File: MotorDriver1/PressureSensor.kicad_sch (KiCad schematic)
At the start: 6 parts

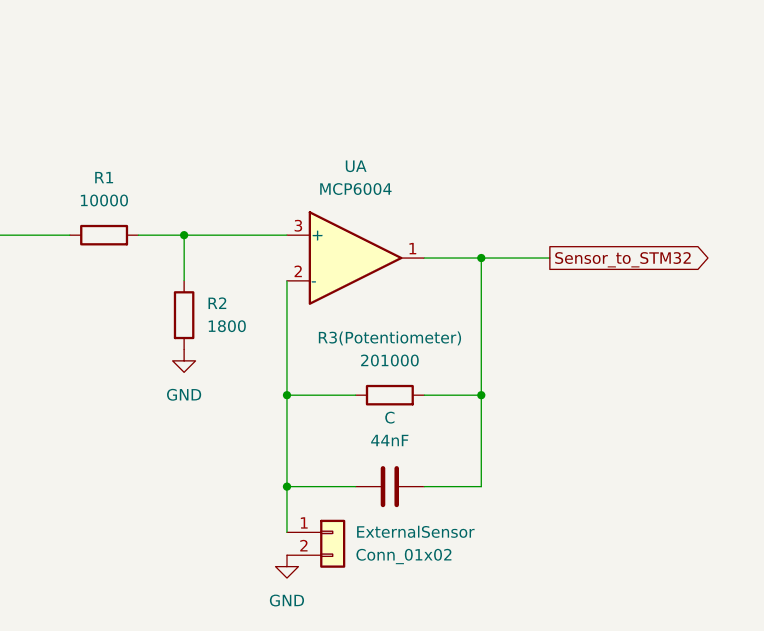
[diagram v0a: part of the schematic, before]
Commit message: added op amp rails
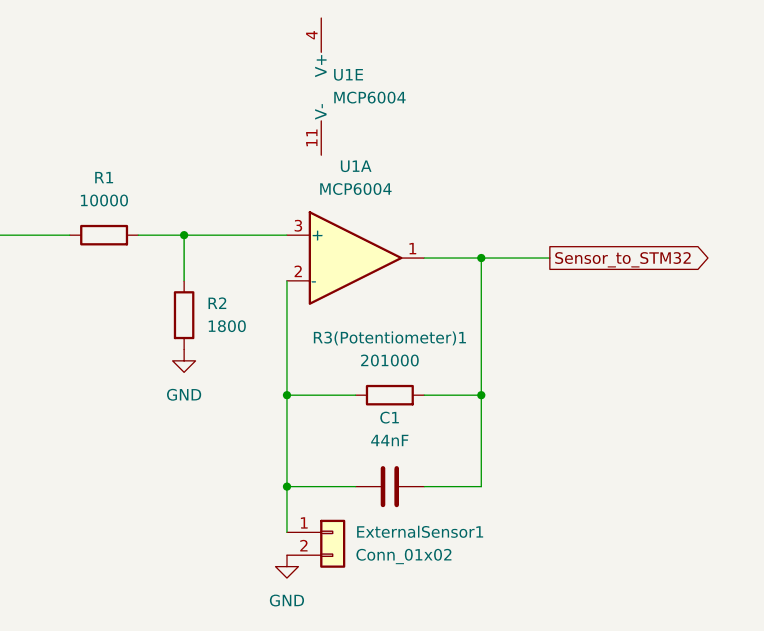
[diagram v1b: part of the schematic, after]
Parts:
- added unit 5 of U1
- renumbered C to C1, ExternalSensor to ExternalSensor1, R3(Potentiometer) to R3(Potentiometer)1, U to U1
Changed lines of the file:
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@@
 		(dnp no)
 		(fields_autoplaced yes)
-		(property "Reference" "ExternalSensor"
+		(property "Reference" "ExternalSensor1"
 			(at 130.81 118.1099 0)
 			(effects
@@
 			(project "PressureSensor"
 				(path "/6b4e6891-da04-4823-bd63-d61c29aaa975"
-					(reference "ExternalSensor")
+					(reference "ExternalSensor1")
 					(unit 1)
 				)
@@
 		(dnp no)
 		(fields_autoplaced yes)
-		(property "Reference" "U"
+		(property "Reference" "U1"
 			(at 130.81 77.47 0)
 			(effects
@@
 			(project "PressureSensor"
 				(path "/6b4e6891-da04-4823-bd63-d61c29aaa975"
-					(reference "U")
+					(reference "U1")
 					(unit 1)
 				)
@@
 	)
 	(symbol
+		(lib_id "Amplifier_Operational:MCP6004")
+		(at 129.54 68.58 0)
+		(unit 5)
+		(exclude_from_sim no)
+		(in_bom yes)
+		(on_board yes)
+		(dnp no)
+		(fields_autoplaced yes)
+		(property "Reference" "U1"
+			(at 128.27 67.3099 0)
+			(effects
+				(font
+					(size 1.27 1.27)
+				)
+				(justify left)
+			)
+		)
+		(property "Value" "MCP6004"
+			(at 128.27 69.8499 0)
+			(effects
+				(font
+					(size 1.27 1.27)
+				)
+				(justify left)
+			)
+		)
+		(property "Footprint" ""
+			(at 128.27 66.04 0)
+			(effects
+				(font
+					(size 1.27 1.27)
+				)
+				(hide yes)
+			)
+		)
+		(property "Datasheet" "http://ww1.microchip.com/downloads/en/DeviceDoc/21733j.pdf"
+			(at 130.81 63.5 0)
+			(effects
+				(font
+					(size 1.27 1.27)
+				)
+				(hide yes)
+			)
+		)
+		(property "Description" "1MHz, Low-Power Op Amp, DIP-14/SOIC-14/TSSOP-14"
+			(at 129.54 68.58 0)
+			(effects
+				(font
+					(size 1.27 1.27)
+				)
+				(hide yes)
+			)
+		)
+		(pin "13"
+		)
+		(pin "11"
+		)
+		(pin "6"
+		)
+		(pin "5"
+		)
+		(pin "1"
+		)
+		(pin "7"
+		)
+		(pin "9"
+		)
+		(pin "4"
+		)
+		(pin "8"
+		)
+		(pin "10"
+		)
+		(pin "12"
+		)
+		(pin "3"
+		)
+		(pin "2"
+		)
+		(pin "14"
+		)
+		(instances
+			(project ""
+				(path "/6b4e6891-da04-4823-bd63-d61c29aaa975"
+					(reference "U1")
+					(unit 5)
+				)
+			)
+		)
+	)
+	(symbol
 		(lib_id "Device:C")
 		(at 134.62 113.03 90)
@@
 		(dnp no)
 		(fields_autoplaced yes)
-		(property "Reference" "C"
+		(property "Reference" "C1"
 			(at 134.62 105.41 90)
 			(effects
@@
 			(project "PressureSensor"
 				(path "/6b4e6891-da04-4823-bd63-d61c29aaa975"
-					(reference "C")
+					(reference "C1")
 					(unit 1)
 				)
@@
 		(dnp no)
 		(fields_autoplaced yes)
-		(property "Reference" "R3(Potentiometer)"
+		(property "Reference" "R3(Potentiometer)1"
 			(at 134.62 96.52 90)
 			(effects
@@
 			(project "PressureSensor"
 				(path "/6b4e6891-da04-4823-bd63-d61c29aaa975"
-					(reference "R3(Potentiometer)")
-					(unit 1)
-				)
+					(reference "R3(Potentiometer)1")
+					(unit 1)
+				)

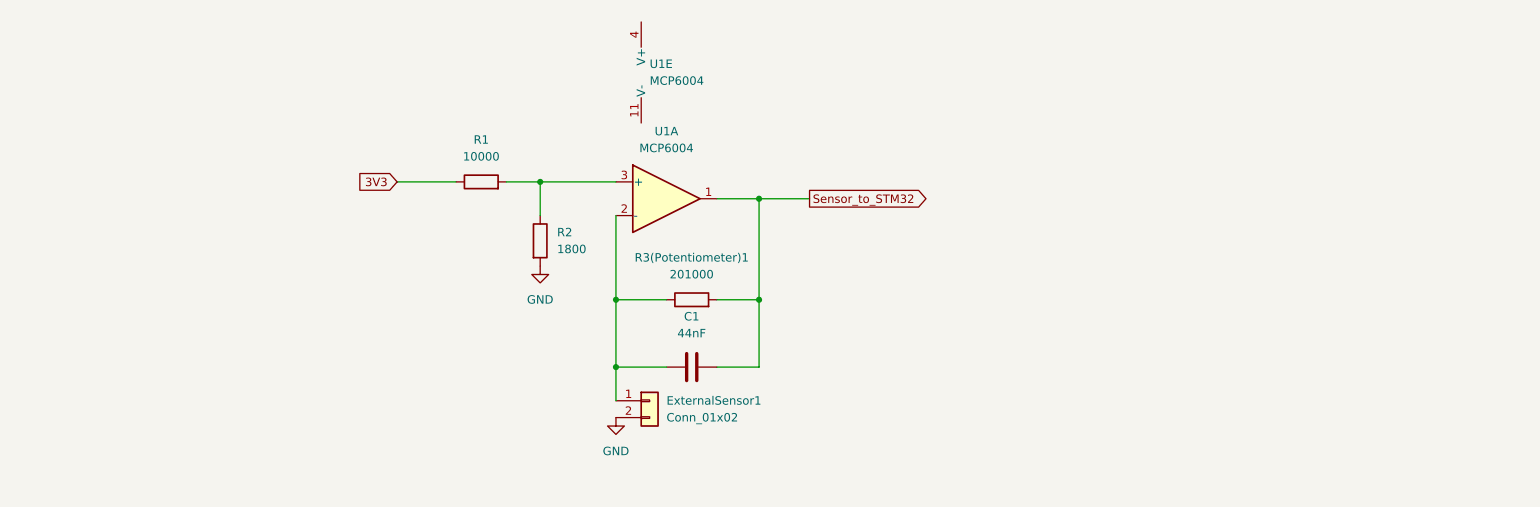
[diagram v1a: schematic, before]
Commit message: updated motor and sensor schematics and added footprints
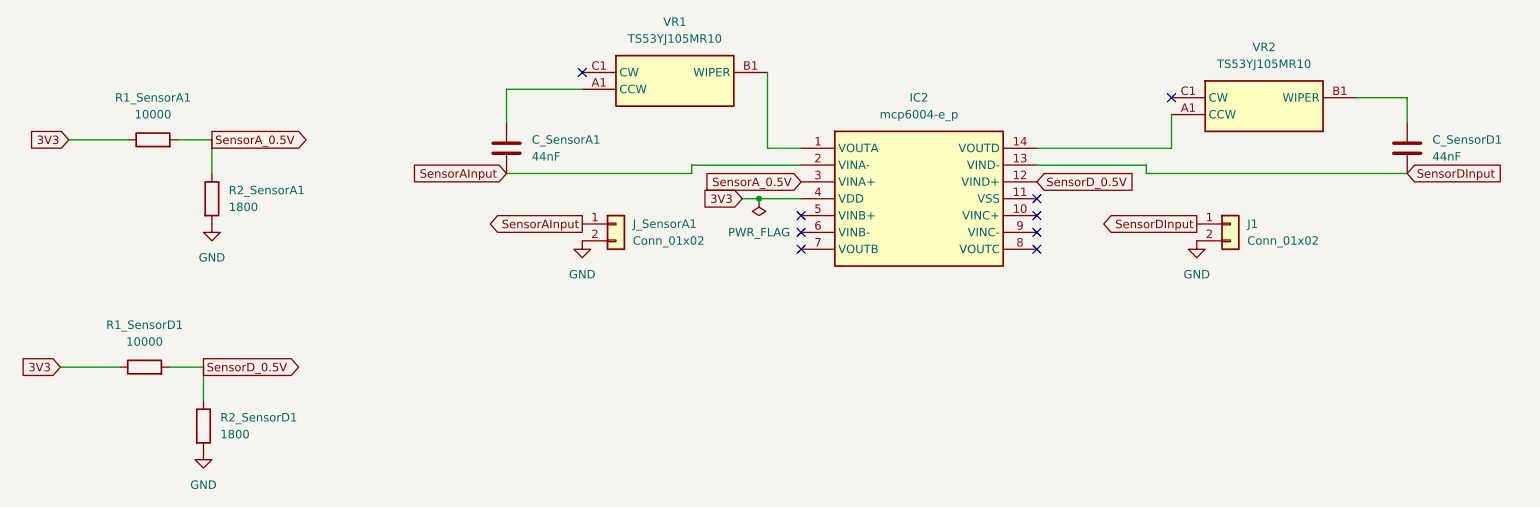
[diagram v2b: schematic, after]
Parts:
- removed C1: 44nF, symbol Device:C
- removed ExternalSensor1: Conn_01x02, symbol Connector_Generic:Conn_01x02
- removed R1: 10000, symbol Device:R
- removed R2: 1800, symbol Device:R
- removed R3(Potentiometer)1: 201000, symbol Device:R
- removed U1: MCP6004, symbol Amplifier_Operational:MCP6004
- added C_SensorA1, C_SensorD1: 44nF, Capacitor_SMD:C_0201_0603Metric, symbol Device:C
- added IC2: mcp6004-e_p, symbol pcb:mcp6004-e_p
- added J1, J_SensorA1: Conn_01x02, symbol Connector_Generic:Conn_01x02
- added R1_SensorA1, R1_SensorD1: 10000, symbol Device:R
- added R2_SensorA1, R2_SensorD1: 1800, symbol Device:R
- added VR1, VR2: TS53YJ105MR10, symbol pcb:TS53YJ105MR10
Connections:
- net 3V3: now also IC2.4 (VDD), R1_SensorA1.1, R1_SensorD1.1
- net GND: now also J1.2 (Pin_2), J_SensorA1.2 (Pin_2), R2_SensorA1.2, R2_SensorD1.2
- new net: IC2.1 (VOUTA), VR1.B1 (WIPER)
- new net: IC2.14 (VOUTD), VR2.A1 (CCW)
- new net: C_SensorA1.2, VR1.A1 (CCW)
- new net: C_SensorD1.2, VR2.B1 (WIPER)
- new net SensorAInput: C_SensorA1.1, IC2.2 (VINA-), J_SensorA1.1 (Pin_1)
- new net SensorA_0.5V: IC2.3 (VINA+), R1_SensorA1.2, R2_SensorA1.1
- new net SensorDInput: C_SensorD1.1, IC2.13 (VIND-), J1.1 (Pin_1)
- new net SensorD_0.5V: IC2.12 (VIND+), R1_SensorD1.2, R2_SensorD1.1
- no-connect marks 0 -> 9

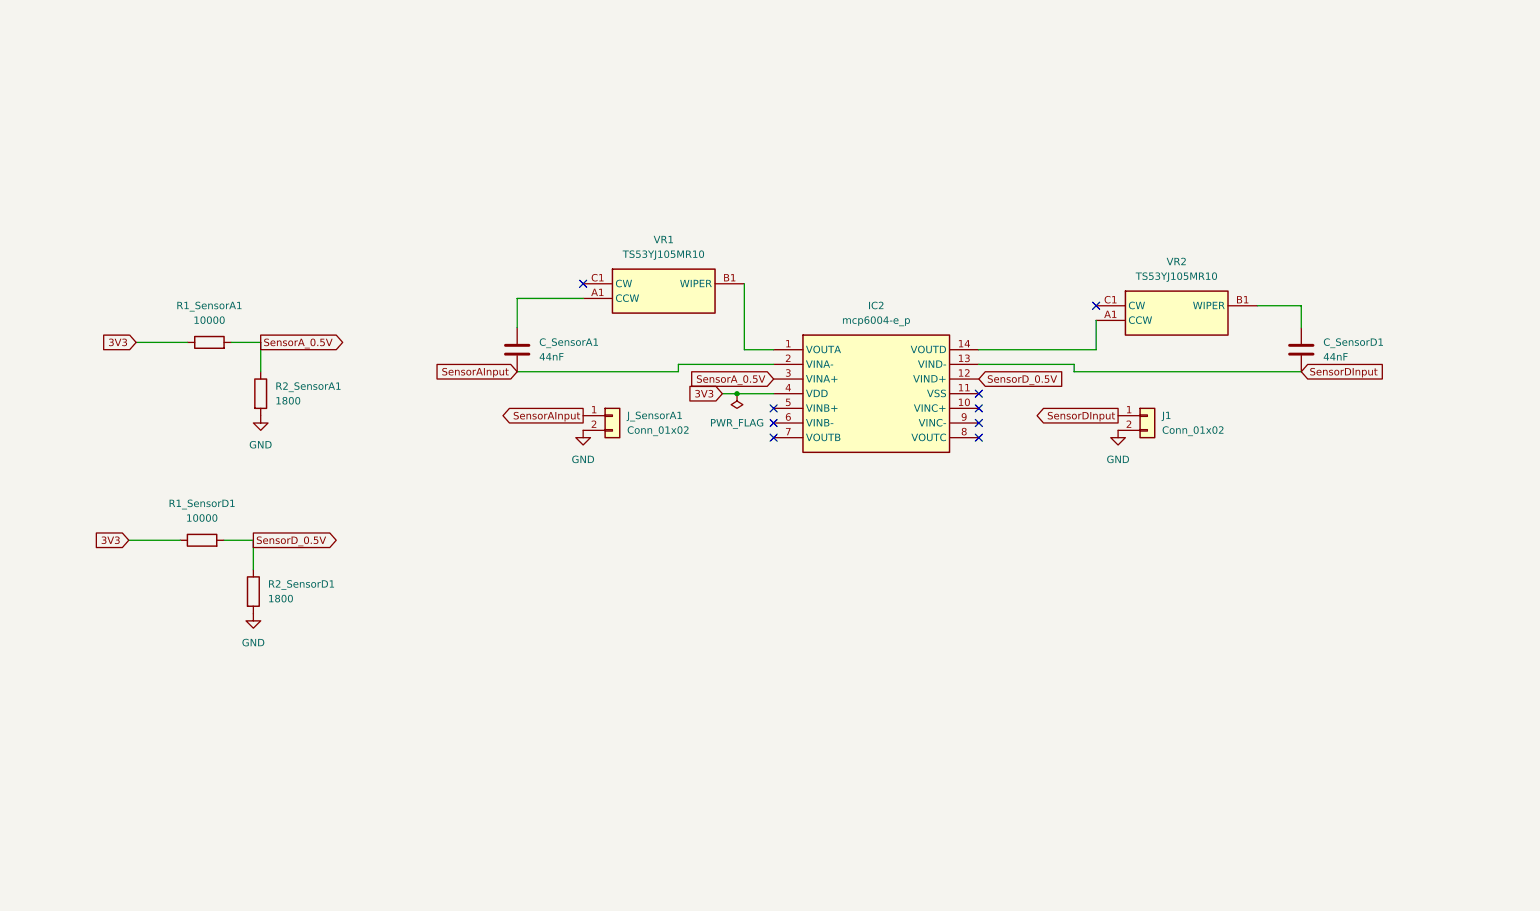
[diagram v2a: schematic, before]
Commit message: missing crystal verification
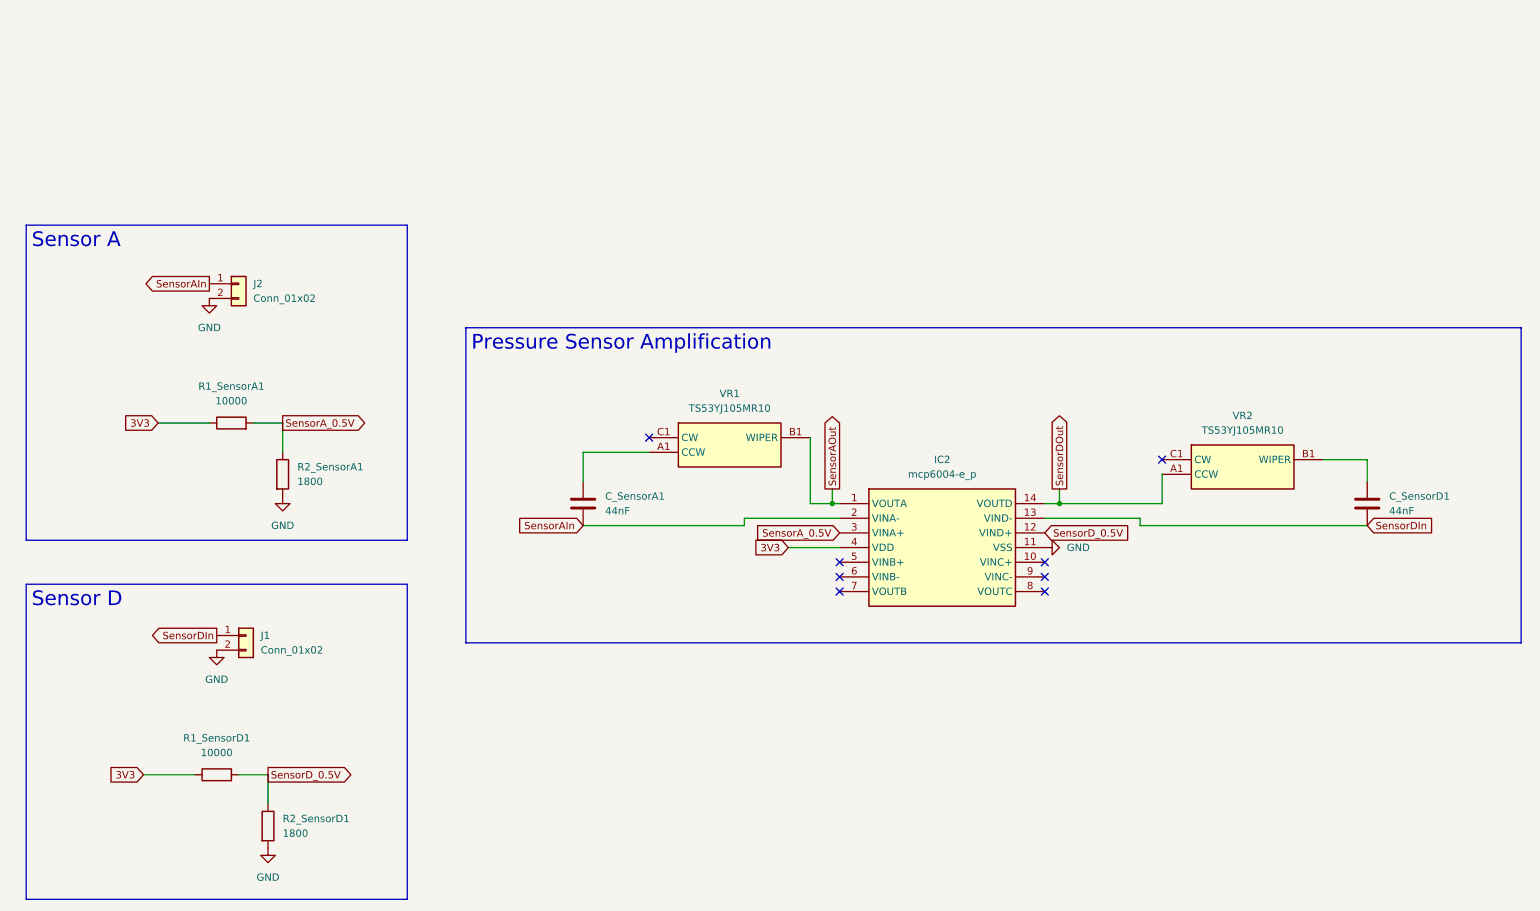
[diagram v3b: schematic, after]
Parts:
- renumbered J_SensorA1 to J2
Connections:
- net GND: now also IC2.11 (VSS)
- net SensorAOut: now reaches IC2.1 (VOUTA), VR1.B1 (WIPER)
- net SensorDOut: now reaches IC2.14 (VOUTD), VR2.A1 (CCW)
- net SensorAInput renamed SensorAIn
- net SensorDInput renamed SensorDIn
- no-connect marks 9 -> 8
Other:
- moved on the sheet: C_SensorA1, C_SensorD1, IC2, J1, J2, R1_SensorA1, R1_SensorD1, R2_SensorA1, R2_SensorD1, VR1, VR2

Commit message: Updated footprints
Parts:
- renumbered IC2 to IC3, J1 to J3
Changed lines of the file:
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@@
 		(dnp no)
 		(fields_autoplaced yes)
-		(property "Reference" "#PWR022"
+		(property "Reference" "#PWR042"
 			(at 63.5 172.72 0)
 			(effects
@@
 			(project "MotorDriver1"
 				(path "/79cc9cfe-04d6-4d00-aa84-feae66cf8c45/309a6c57-e91b-42c8-8b29-fcecc8b43c4f"
-					(reference "#PWR022")
+					(reference "#PWR042")
 					(unit 1)
 				)
@@
 		(dnp no)
 		(fields_autoplaced yes)
-		(property "Reference" "#PWR025"
+		(property "Reference" "#PWR041"
 			(at 54.61 138.43 0)
 			(effects
@@
 			(project "MotorDriver1"
 				(path "/79cc9cfe-04d6-4d00-aa84-feae66cf8c45/309a6c57-e91b-42c8-8b29-fcecc8b43c4f"
-					(reference "#PWR025")
+					(reference "#PWR041")
 					(unit 1)
 				)
@@
 		(dnp no)
 		(fields_autoplaced yes)
-		(property "Reference" "#PWR023"
+		(property "Reference" "#PWR043"
 			(at 66.04 111.76 0)
 			(effects
@@
 			(project "MotorDriver1"
 				(path "/79cc9cfe-04d6-4d00-aa84-feae66cf8c45/309a6c57-e91b-42c8-8b29-fcecc8b43c4f"
-					(reference "#PWR023")
+					(reference "#PWR043")
 					(unit 1)
 				)
@@
 		(dnp no)
 		(fields_autoplaced yes)
-		(property "Reference" "#PWR024"
+		(property "Reference" "#PWR040"
 			(at 53.34 77.47 0)
 			(effects
@@
 			(project "MotorDriver1"
 				(path "/79cc9cfe-04d6-4d00-aa84-feae66cf8c45/309a6c57-e91b-42c8-8b29-fcecc8b43c4f"
-					(reference "#PWR024")
+					(reference "#PWR040")
 					(unit 1)
 				)
@@
 		(dnp no)
 		(fields_autoplaced yes)
-		(property "Reference" "IC2"
+		(property "Reference" "IC3"
 			(at 180.34 99.06 0)
 			(effects
@@
 			(project ""
 				(path "/79cc9cfe-04d6-4d00-aa84-feae66cf8c45/309a6c57-e91b-42c8-8b29-fcecc8b43c4f"
-					(reference "IC2")
+					(reference "IC3")
 					(unit 1)
 				)
@@
 		(dnp no)
 		(fields_autoplaced yes)
-		(property "Reference" "#PWR036"
+		(property "Reference" "#PWR044"
 			(at 204.47 114.3 0)
 			(effects
@@
 			(project "MotorDriver1"
 				(path "/79cc9cfe-04d6-4d00-aa84-feae66cf8c45/309a6c57-e91b-42c8-8b29-fcecc8b43c4f"
-					(reference "#PWR036")
+					(reference "#PWR044")
 					(unit 1)
 				)
@@
 		(dnp no)
 		(fields_autoplaced yes)
-		(property "Reference" "J1"
+		(property "Reference" "J3"
 			(at 62.23 129.5399 0)
 			(effects
@@
 			(project "MotorDriver1"
 				(path "/79cc9cfe-04d6-4d00-aa84-feae66cf8c45/309a6c57-e91b-42c8-8b29-fcecc8b43c4f"
-					(reference "J1")
-					(unit 1)
-				)
+					(reference "J3")
+					(unit 1)
+				)

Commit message: laid out PCB
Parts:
- IC2: renamed from IC3; footprint (none) -> footprintLib:DIP781W56P254L1918H533Q14N
- J2, J3: footprint (none) -> Connector_PinHeader_2.54mm:PinHeader_1x02_P2.54mm_Vertical
- R16: renamed from R1_SensorD1; footprint (none) -> Resistor_SMD:R_0402_1005Metric
- R17: renamed from R1_SensorA1; footprint (none) -> Resistor_SMD:R_0402_1005Metric
- R18: renamed from R2_SensorD1; footprint (none) -> Resistor_SMD:R_0402_1005Metric
- R19: renamed from R2_SensorA1; footprint (none) -> Resistor_SMD:R_0402_1005Metric
- VR1, VR2: footprint (none) -> footprintLib:TS53YJ105MR10
- renumbered C_SensorA1 to C_A1, C_SensorD1 to C_D1
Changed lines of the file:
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@@
 		(dnp no)
 		(fields_autoplaced yes)
-		(property "Reference" "R2_SensorA1"
+		(property "Reference" "R19"
 			(at 68.58 100.3299 0)
 			(effects
@@
 			)
 		)
-		(property "Footprint" ""
+		(property "Footprint" "Resistor_SMD:R_0402_1005Metric"
 			(at 64.262 101.6 90)
 			(effects
@@
 			(project "MotorDriver1"
 				(path "/79cc9cfe-04d6-4d00-aa84-feae66cf8c45/309a6c57-e91b-42c8-8b29-fcecc8b43c4f"
-					(reference "R2_SensorA1")
+					(reference "R19")
 					(unit 1)
 				)
@@
 		(on_board yes)
 		(dnp no)
-		(property "Reference" "R1_SensorA1"
+		(property "Reference" "R17"
 			(at 57.15 86.36 90)
 			(effects
@@
 			)
 		)
-		(property "Footprint" ""
+		(property "Footprint" "Resistor_SMD:R_0402_1005Metric"
 			(at 57.15 94.488 90)
 			(effects
@@
 			(project "MotorDriver1"
 				(path "/79cc9cfe-04d6-4d00-aa84-feae66cf8c45/309a6c57-e91b-42c8-8b29-fcecc8b43c4f"
-					(reference "R1_SensorA1")
+					(reference "R17")
 					(unit 1)
 				)
@@
 		(on_board yes)
 		(dnp no)
-		(property "Reference" "R1_SensorD1"
+		(property "Reference" "R16"
 			(at 54.61 147.32 90)
 			(effects
@@
 			)
 		)
-		(property "Footprint" ""
+		(property "Footprint" "Resistor_SMD:R_0402_1005Metric"
 			(at 54.61 155.448 90)
 			(effects
@@
 			(project "MotorDriver1"
 				(path "/79cc9cfe-04d6-4d00-aa84-feae66cf8c45/309a6c57-e91b-42c8-8b29-fcecc8b43c4f"
-					(reference "R1_SensorD1")
+					(reference "R16")
 					(unit 1)
 				)
@@
 		(dnp no)
 		(fields_autoplaced yes)
-		(property "Reference" "IC3"
+		(property "Reference" "IC2"
 			(at 180.34 99.06 0)
 			(effects
@@
 			)
 		)
-		(property "Footprint" ""
+		(property "Footprint" "footprintLib:DIP781W56P254L1918H533Q14N"
 			(at 194.31 201.6 0)
 			(effects
@@
 			(project ""
 				(path "/79cc9cfe-04d6-4d00-aa84-feae66cf8c45/309a6c57-e91b-42c8-8b29-fcecc8b43c4f"
-					(reference "IC3")
+					(reference "IC2")
 					(unit 1)
 				)
@@
 		(dnp no)
 		(fields_autoplaced yes)
-		(property "Reference" "R2_SensorD1"
+		(property "Reference" "R18"
 			(at 66.04 161.2899 0)
 			(effects
@@
 			)
 		)
-		(property "Footprint" ""
+		(property "Footprint" "Resistor_SMD:R_0402_1005Metric"
 			(at 61.722 162.56 90)
 			(effects
@@
 			(project "MotorDriver1"
 				(path "/79cc9cfe-04d6-4d00-aa84-feae66cf8c45/309a6c57-e91b-42c8-8b29-fcecc8b43c4f"
-					(reference "R2_SensorD1")
+					(reference "R18")
 					(unit 1)
 				)
@@
 			)
 		)
-		(property "Footprint" ""
+		(property "Footprint" "Connector_PinHeader_2.54mm:PinHeader_1x02_P2.54mm_Vertical"
 			(at 59.69 129.54 0)
 			(effects
@@
 		(dnp no)
 		(fields_autoplaced yes)
-		(property "Reference" "C_SensorA1"
+		(property "Reference" "C_A1"
 			(at 121.92 105.4099 0)
 			(effects
@@
 			(project "MotorDriver1"
 				(path "/79cc9cfe-04d6-4d00-aa84-feae66cf8c45/309a6c57-e91b-42c8-8b29-fcecc8b43c4f"
-					(reference "C_SensorA1")
+					(reference "C_A1")
 					(unit 1)
 				)
@@
 		(dnp no)
 		(fields_autoplaced yes)
-		(property "Reference" "C_SensorD1"
+		(property "Reference" "C_D1"
 			(at 257.81 105.4099 0)
 			(effects
@@
 			(project "MotorDriver1"
 				(path "/79cc9cfe-04d6-4d00-aa84-feae66cf8c45/309a6c57-e91b-42c8-8b29-fcecc8b43c4f"
-					(reference "C_SensorD1")
+					(reference "C_D1")
 					(unit 1)
 				)
@@
 			)
 		)
-		(property "Footprint" ""
+		(property "Footprint" "Connector_PinHeader_2.54mm:PinHeader_1x02_P2.54mm_Vertical"
 			(at 58.42 68.58 0)
 			(effects
@@
 			)
 		)
-		(property "Footprint" ""
+		(property "Footprint" "footprintLib:TS53YJ105MR10"
 			(at 242.57 193.98 0)
 			(effects
@@
 			)
 		)
-		(property "Footprint" ""
+		(property "Footprint" "footprintLib:TS53YJ105MR10"
 			(at 153.67 190.17 0)
 			(effects
